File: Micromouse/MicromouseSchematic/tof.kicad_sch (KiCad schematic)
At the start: 7 parts

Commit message: tof version 1
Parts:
- removed C?: 4.7 μF, symbol Device:C
- removed C?: 100nF, symbol Device:C
- removed R? (x4): 47kΩ, symbol Device:R
- removed U?: VL6180V1NR_1, VL6180V1NR_1:XDCR_VL6180V1NR_1, symbol VL6180:VL6180V1NR_1
- added C10, C15, C16, C9: 4.7uF, symbol Device:C
- added C11, C12, C17, C18: 100nF, symbol Device:C
- added C13, C14, C8: 10uF, symbol Device:C
- added R1, R10, R11, R12, R13, R14, R15, R16, R17, R18, R19, R2, R3, R4, R5, R6, R7, R8, R9: 47k, symbol Device:R
- added U1, U10, U2, U9: VL6180V1NR_1, VL6180V1NR_1:XDCR_VL6180V1NR_1, symbol VL6180V1NR_1:VL6180V1NR_1
- added U6: TCA9544APWR, TCA9544APWR:SOP65P640X120-20N, symbol TCA9544APWR:TCA9544APWR
- added U8: LP5907MFX-2.8_NOPB, LP5907MFX_2_8_NOPB:SOT95P280X145-5N, symbol LP5907MFX-2.8_NOPB:LP5907MFX-2.8_NOPB
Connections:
- net GND: now also C10.2, C11.2, C12.2, C13.2, C14.2, C15.2, C16.2, C17.2, C18.2, C8.2, C9.2, U1.12 (GND), U1.9 (AVSS_VCSEL), U10.12 (GND), U10.9 (AVSS_VCSEL), U2.12 (GND), U2.9 (AVSS_VCSEL), U6.1 (A0), U6.10 (GND), U6.2 (A1), U6.3 (A2), U8.2 (GND), U9.12 (GND), U9.9 (AVSS_VCSEL)
- net SCL (ToF): now also R6.2, U6.18 (SCL)
- net SDA (ToF): now also R5.2, U6.19 (SDA)
- new net: R10.2, U1.4 (GPIO0/CE)
- new net: R18.2, U9.4 (GPIO0/CE)
- new net: R11.2, U2.4 (GPIO0/CE)
- new net: R19.2, U10.4 (GPIO0/CE)
- new net 2V8: C10.1, C11.1, C12.1, C14.1, C15.1, C16.1, C17.1, C18.1, C9.1, R1.1, R10.1, R11.1, R12.1, R13.1, R14.1, R15.1, R16.1, R17.1, R18.1, R19.1, R2.1, R3.1, R4.1, R8.1, R9.1, U1.10 (AVDD), U1.8 (AVDD_VCSEL), U10.10 (AVDD), U10.8 (AVDD_VCSEL), U2.10 (AVDD), U2.8 (AVDD_VCSEL), U8.5 (OUT), U9.10 (AVDD), U9.8 (AVDD_VCSEL)
- new net 3V3: C13.1, C8.1, R5.1, R6.1, R7.1, U6.20 (VCC), U8.1 (IN), U8.3 (EN)
- new net INT (ToF): R7.2, U6.17 (~{INT})
- new net INT0: R8.2, U1.1 (GPIO1), U6.4 (~{INT0})
- new net INT1: R16.2, U6.7 (~{INT1}), U9.1 (GPIO1)
- new net INT2: R9.2, U2.1 (GPIO1), U6.11 (~{INT2})
- new net INT3: R17.2, U10.1 (GPIO1), U6.14 (~{INT3})
- new net SC0: R1.2, U1.5 (SCL), U6.6 (SC0)
- new net SC1: R12.2, U6.9 (SC1), U9.5 (SCL)
- new net SC2: R2.2, U2.5 (SCL), U6.13 (SC2)
- new net SC3: R13.2, U10.5 (SCL), U6.16 (SC3)
- new net SD0: R3.2, U1.6 (SDA), U6.5 (SD0)
- new net SD1: R14.2, U6.8 (SD1), U9.6 (SDA)
- new net SD2: R4.2, U2.6 (SDA), U6.12 (SD2)
- new net SD3: R15.2, U10.6 (SDA), U6.15 (SD3)
- no-connect marks 0 -> 1
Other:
- note added: "2V8 Linear Regulator"
- note added: "I2C Multiplexer"
- note added: "TOF 0"
- note added: "TOF 1"
- note added: "TOF 2"
- note added: "TOF 3"
- note removed: "ToF"

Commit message: added some stuff
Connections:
- net 2V8 renamed +2.8V
- net 3V3 renamed +3.3V

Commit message: Micromouse KiCad: MP6550 libs in project, fp-lib paths, schematic updates
Move MP6550G-Z symbol and legacy footprints into MicromouseSchematic, add
MP6550G-Z.pretty with MP6550_MNP footprint, and point fp-lib-table at the
project-local MM_MP6550G-Z library.

Replace old absolute footprint paths with this repo’s Micromouse tree and
MM_* library names. Update root schematic and IMU/IR/motor/TOF/regulator
subsheets; add empty bluethooth.kicad_sch hierarchical sheet. Extend KiCad
project BOM field configuration; refresh fp-info-cache. Drop schematic lock
file; include dated schematic backup zip.
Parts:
- U8: footprint LP5907MFX_2_8_NOPB:SOT95P280X145-5N -> LP5907MFX-2.8_NOPB:SOT95P280X145-5N
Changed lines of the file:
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@@
 			)
 		)
-		(property "Footprint" "LP5907MFX_2_8_NOPB:SOT95P280X145-5N"
+		(property "Footprint" "LP5907MFX-2.8_NOPB:SOT95P280X145-5N"
 			(at 189.23 133.35 0)
 			(effects

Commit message: Micromouse KiCad: STM32-centric routing; ERC errors 23→6; backups and gitignore
Body:
Connected almost all STM32 signals; ERC down to 6

Rework root schematic plus motor driver, IMU/magnetometer, IR sensor, and TOF
subsheets so the bulk of signals reach the STM32. KiCad ERC is not fully clean
yet, but major nets are in place: errors dropped from 23 to 6 while many
previously unconnected signals were wired.

Add 2026-04-08 schematic backup zips. Extend .gitignore for macOS .DS_Store
paths. Update MicromouseSchematic.kicad_prl.
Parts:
- U1: footprint VL6180V1NR_1:XDCR_VL6180V1NR_1 -> MM_VL6180V1NR_1:XDCR_VL6180V1NR_1
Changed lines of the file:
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@@
 			)
 		)
-		(property "Footprint" "VL6180V1NR_1:XDCR_VL6180V1NR_1"
+		(property "Footprint" "MM_VL6180V1NR_1:XDCR_VL6180V1NR_1"
 			(at 78.74 43.18 0)
 			(effects

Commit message: Micromouse KiCad: MP6550 layout, schematic updates; ERC clean, warnings ~5–6
Relocate MP6550G-Z symbol and footprint trees from MicromouseSchematic into
Micromouse/MP6550G-Z and refresh sym-lib-table (portable ${KIPRJMOD} paths
where applicable, MP6550 at new location).

Update root schematic plus IMU, IR, motor driver, and TOF subsheets. KiCad
ERC: all errors resolved (previously 6 remaining after earlier bring-up).
Warnings reduced from roughly 35–40+ down to about 5–6.

Add MicromouseSchematic-2026-04-11_212024.zip backup.
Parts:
- U10, U2, U9: footprint VL6180V1NR_1:XDCR_VL6180V1NR_1 -> MM_VL6180V1NR_1:XDCR_VL6180V1NR_1
- U6: footprint TCA9544APWR:SOP65P640X120-20N -> MM_TCA9544APWR:SOP65P640X120-20N
- U8: footprint LP5907MFX-2.8_NOPB:SOT95P280X145-5N -> MM_LP5907MFX_2_8_NOPB:SOT95P280X145-5N
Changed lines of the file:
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@@
 			)
 		)
-		(property "Footprint" "VL6180V1NR_1:XDCR_VL6180V1NR_1"
+		(property "Footprint" "MM_VL6180V1NR_1:XDCR_VL6180V1NR_1"
 			(at 196.85 43.18 0)
 			(effects
@@
 			)
 		)
-		(property "Footprint" "VL6180V1NR_1:XDCR_VL6180V1NR_1"
+		(property "Footprint" "MM_VL6180V1NR_1:XDCR_VL6180V1NR_1"
 			(at 78.74 90.17 0)
 			(effects
@@
 			)
 		)
-		(property "Footprint" "VL6180V1NR_1:XDCR_VL6180V1NR_1"
+		(property "Footprint" "MM_VL6180V1NR_1:XDCR_VL6180V1NR_1"
 			(at 196.85 90.17 0)
 			(effects
@@
 			)
 		)
-		(property "Footprint" "TCA9544APWR:SOP65P640X120-20N"
+		(property "Footprint" "MM_TCA9544APWR:SOP65P640X120-20N"
 			(at 127 156.21 0)
 			(effects
@@
 			)
 		)
-		(property "Footprint" "LP5907MFX-2.8_NOPB:SOT95P280X145-5N"
+		(property "Footprint" "MM_LP5907MFX_2_8_NOPB:SOT95P280X145-5N"
 			(at 189.23 133.35 0)
 			(effects

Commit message: assigned capacitor footprints. still have to figure out rest
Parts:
- C10, C11, C12, C15, C16, C17, C18, C9: footprint (none) -> Capacitor_SMD:C_0402_1005Metric
- C13, C14, C8: footprint (none) -> Capacitor_SMD:C_0805_2012Metric
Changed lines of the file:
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@@
 			)
 		)
-		(property "Footprint" ""
+		(property "Footprint" "Capacitor_SMD:C_0402_1005Metric"
 			(at 241.3 79.0448 0)
 			(effects
@@
 			)
 		)
-		(property "Footprint" ""
+		(property "Footprint" "Capacitor_SMD:C_0805_2012Metric"
 			(at 105.1052 132.08 0)
 			(effects
@@
 			)
 		)
-		(property "Footprint" ""
+		(property "Footprint" "Capacitor_SMD:C_0805_2012Metric"
 			(at 213.0552 135.89 0)
 			(effects
@@
 			)
 		)
-		(property "Footprint" ""
+		(property "Footprint" "Capacitor_SMD:C_0402_1005Metric"
 			(at 241.3 32.0548 0)
 			(effects
@@
 			)
 		)
-		(property "Footprint" ""
+		(property "Footprint" "Capacitor_SMD:C_0402_1005Metric"
 			(at 114.3 81.5848 0)
 			(effects
@@
 			)
 		)
-		(property "Footprint" ""
+		(property "Footprint" "Capacitor_SMD:C_0402_1005Metric"
 			(at 123.19 79.0448 0)
 			(effects
@@
 			)
 		)
-		(property "Footprint" ""
+		(property "Footprint" "Capacitor_SMD:C_0402_1005Metric"
 			(at 123.19 32.0548 0)
 			(effects
@@
 			)
 		)
-		(property "Footprint" ""
+		(property "Footprint" "Capacitor_SMD:C_0402_1005Metric"
 			(at 232.41 34.5948 0)
 			(effects
@@
 			)
 		)
-		(property "Footprint" ""
+		(property "Footprint" "Capacitor_SMD:C_0402_1005Metric"
 			(at 114.3 34.5948 0)
 			(effects
@@
 			)
 		)
-		(property "Footprint" ""
+		(property "Footprint" "Capacitor_SMD:C_0402_1005Metric"
 			(at 232.41 81.5848 0)
 			(effects
@@
 			)
 		)
-		(property "Footprint" ""
+		(property "Footprint" "Capacitor_SMD:C_0805_2012Metric"
 			(at 160.9852 138.43 0)
 			(effects

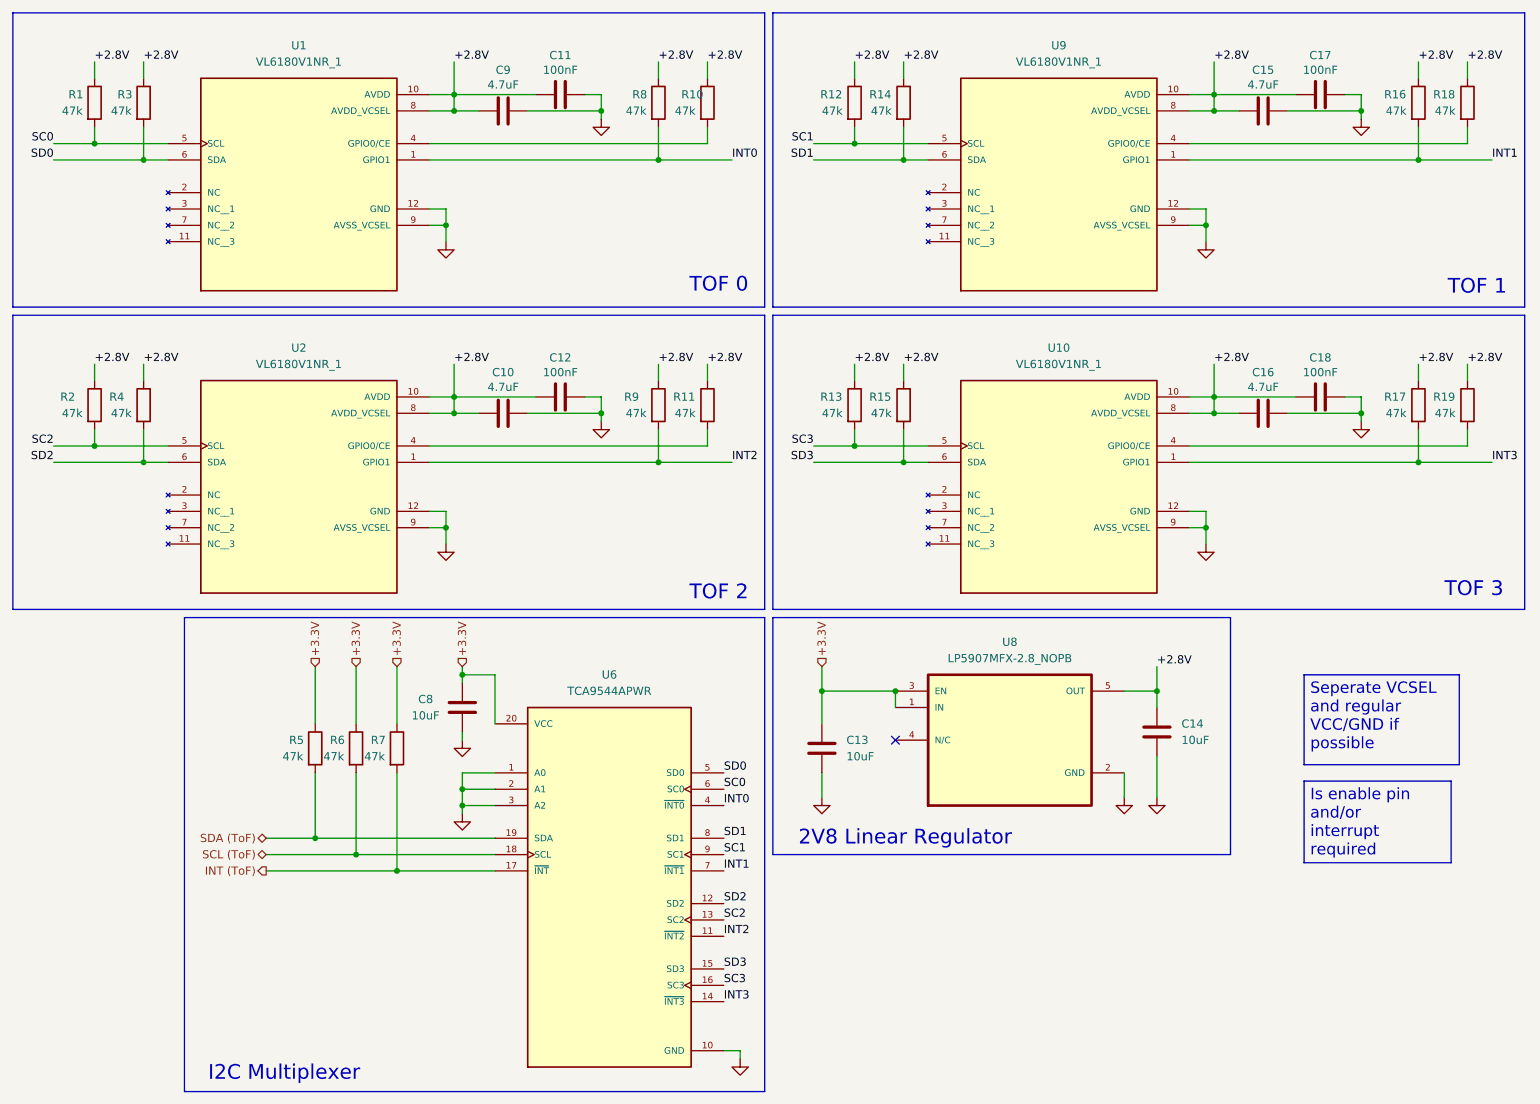
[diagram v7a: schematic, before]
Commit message: Micromouse KiCad: VL53L4 TOF footprint/sym; fp-lib via KICAD_ADDITIONAL_FOOTPRINT
Add UltraLibrarian VL53L4CDV0DH-1 KiCad symbol and LGA12_STM footprint plus
vendor readme; register them in sym-lib-table and fp-lib-table.

Point MM footprint libraries at ${KICAD_ADDITIONAL_FOOTPRINT}/... for
portable paths; add MM_VL53L4CDV0DH-1.

Rework tof.kicad_sch (large cleanup vs embedded library bulk) and touch root
MicromouseSchematic.kicad_sch and MicromouseSchematic.kicad_pro for project
consistency.
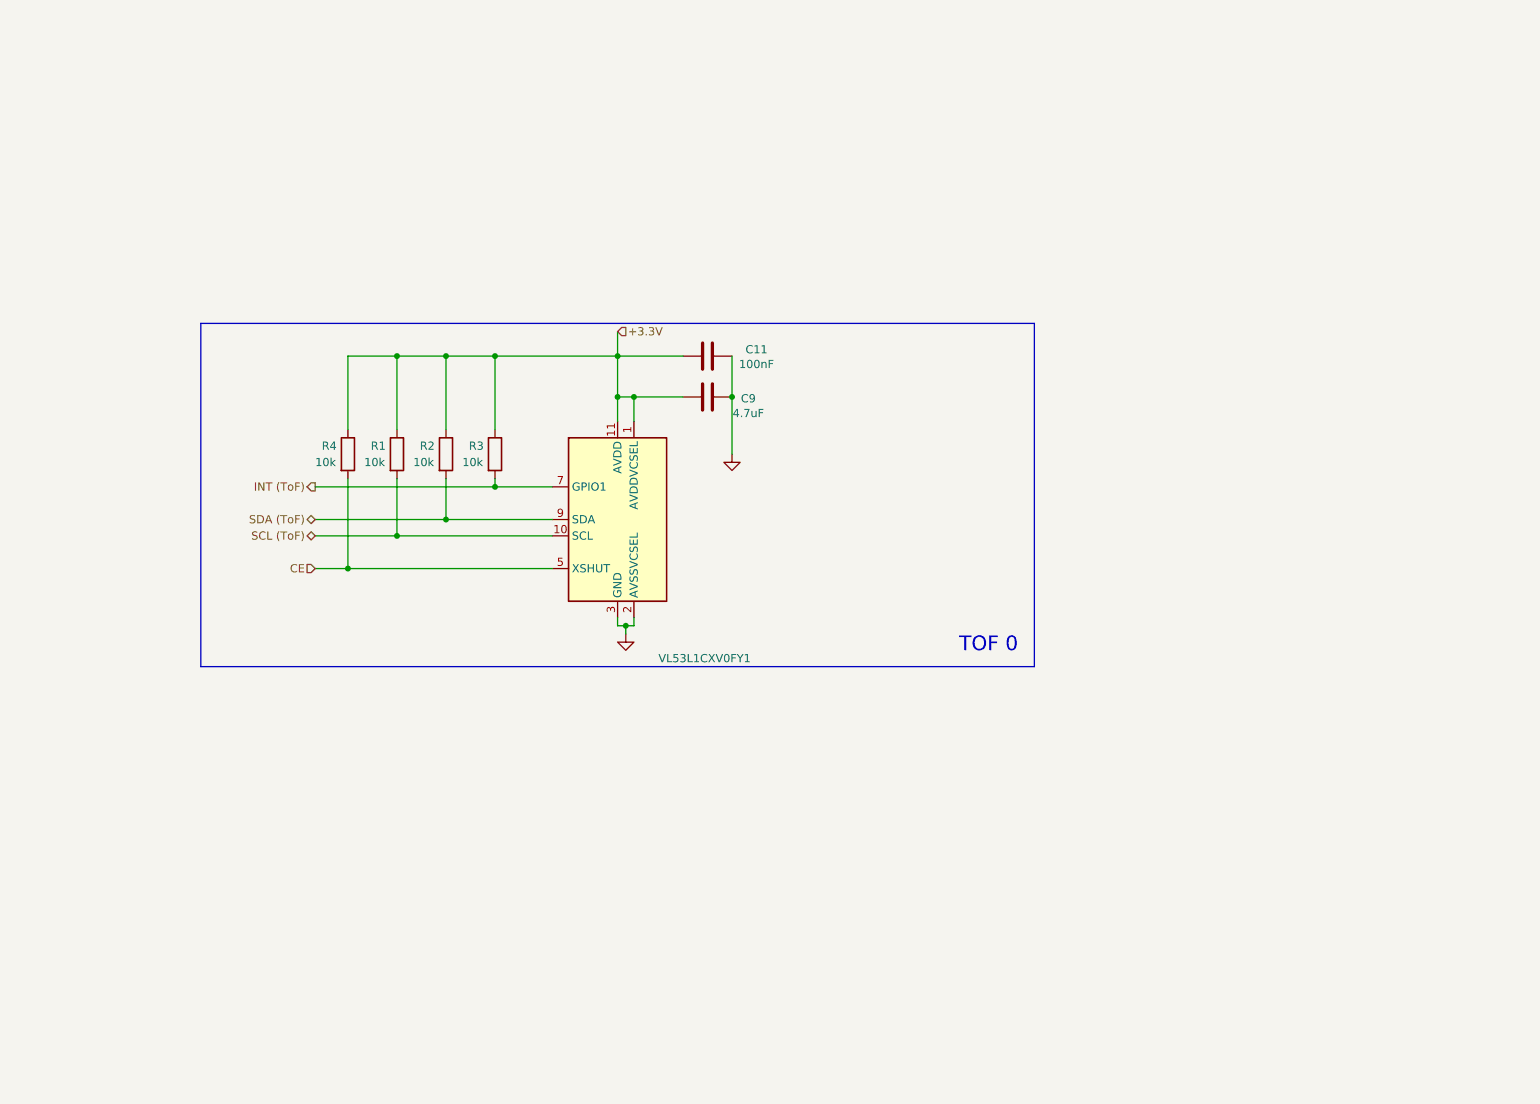
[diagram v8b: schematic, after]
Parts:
- removed C10, C15, C16: 4.7uF, Capacitor_SMD:C_0402_1005Metric, symbol Device:C
- removed C12, C17, C18: 100nF, Capacitor_SMD:C_0402_1005Metric, symbol Device:C
- removed C13, C14, C8: 10uF, Capacitor_SMD:C_0805_2012Metric, symbol Device:C
- removed R10, R11, R12, R13, R14, R15, R16, R17, R18, R19, R5, R6, R7, R8, R9: 47k, symbol Device:R
- removed U1, U10, U2, U9: VL6180V1NR_1, MM_VL6180V1NR_1:XDCR_VL6180V1NR_1, symbol VL6180V1NR_1:VL6180V1NR_1
- removed U6: TCA9544APWR, MM_TCA9544APWR:SOP65P640X120-20N, symbol TCA9544APWR:TCA9544APWR
- removed U8: LP5907MFX-2.8_NOPB, MM_LP5907MFX_2_8_NOPB:SOT95P280X145-5N, symbol LP5907MFX-2.8_NOPB:LP5907MFX-2.8_NOPB
- added U1: VL53L1CXV0FY1, MM_VL53L4CDV0DH-1:LGA12_STM, symbol Sensor_Distance:VL53L1CXV0FY1
- R1, R2, R3, R4: value 47k -> 10k
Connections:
- net +2.8V is gone; now on net +3.3V: C11.1, C9.1, R1.1, R2.1, R3.1, R4.1
- net SC0 is gone; now on net SCL (ToF): R1.2
- net SC2 is gone; now on net SDA (ToF): R2.2
- net SD0 is gone; now on net INT (ToF): R3.2
- net +3.3V: now also U1.1 (AVDDVCSEL), U1.11 (AVDD)
- net GND: now also U1.12 (GND), U1.2 (AVSSVCSEL), U1.3 (GND), U1.4 (GND), U1.6 (GND)
- net INT (ToF): now also U1.7 (GPIO1)
- net SCL (ToF): now also U1.10 (SCL)
- net SDA (ToF): now also U1.9 (SDA)
- net SD2 renamed CE
- net CE: now also U1.5 (XSHUT)
- no-connect marks 1 -> 0
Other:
- note removed: "2V8 Linear Regulator"
- note removed: "I2C Multiplexer"
- note removed: "TOF 1"
- note removed: "TOF 2"
- note removed: "TOF 3"
- moved on the sheet: C11, C9, R1
